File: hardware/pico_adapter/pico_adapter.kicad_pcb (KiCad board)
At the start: 2 copper layers, 13 x 1.4 mm, 43 parts, among them J1 L77HDE15SD1CH4F, J2 AudioJack2_Ground, J3 5V in, Q1 Q_NMOS_DGS, Q2 Q_NMOS_DGS

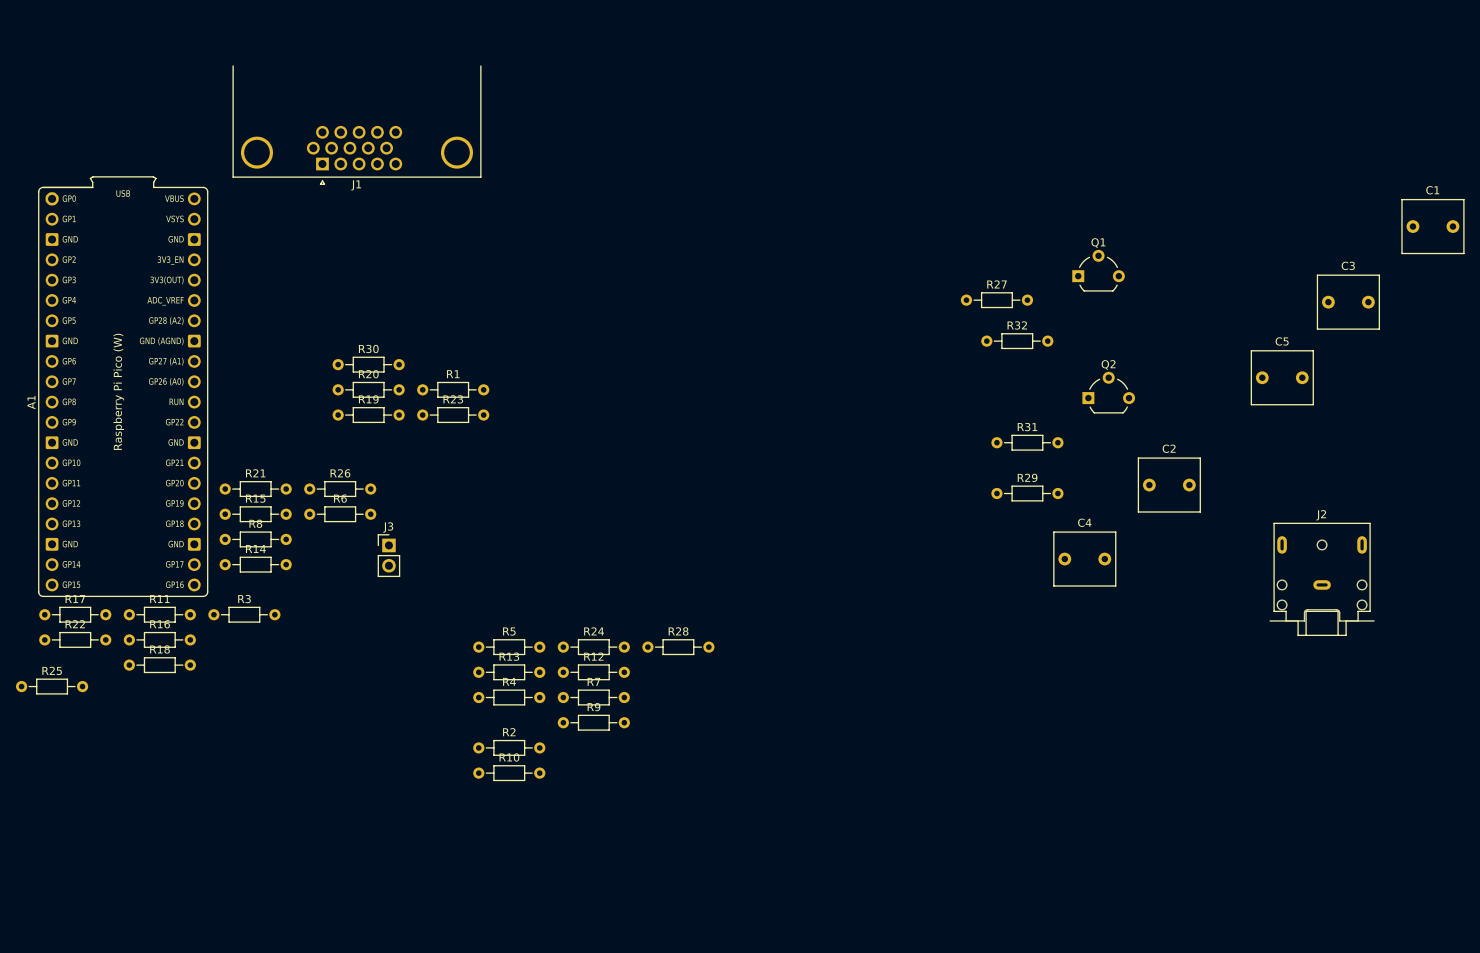
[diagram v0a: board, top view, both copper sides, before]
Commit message: fixed PWR_FLAG in schematic, problem: layout GND area does not fill
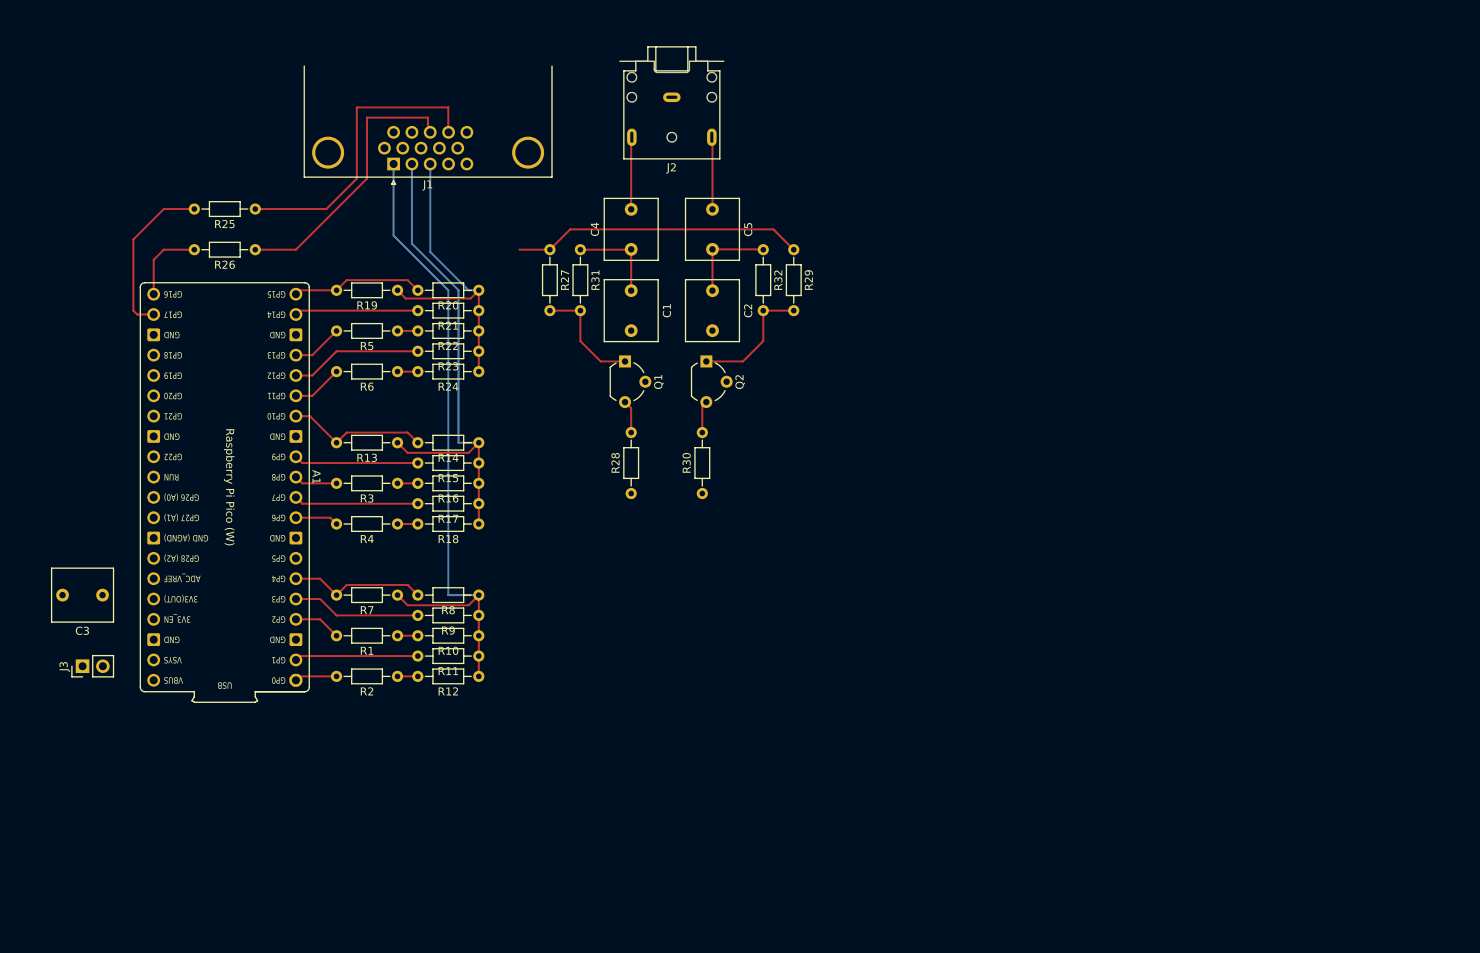
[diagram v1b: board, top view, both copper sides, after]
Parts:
- A1: value RaspberryPi-Pico_Socket -> RaspberryPi-Pico-Socket
- moved C3 157.5 mm to (39.3, 92.7), turned to 180 degrees
- moved J2 101.6 mm to (110.5, 30.5), turned to 180 degrees
- moved C1 98.0 mm to (105.4, 54.6), turned to -90 degrees
- moved C5 71.9 mm to (115.6, 44.5), turned to -90 degrees
- moved A1 67.5 mm to (63.5, 103.4), turned to 180 degrees
- moved C4 66.6 mm to (105.4, 49.5), turned to 90 degrees
- moved R22 66.6 mm to (86.4, 59.7), turned to 180 degrees
- moved R25 66.5 mm to (58.4, 44.5), turned to 180 degrees
- moved C2 59.8 mm to (115.6, 54.6), turned to -90 degrees
- moved Q1 57.6 mm to (104.6, 63.5), turned to -90 degrees
- moved R31 57.4 mm to (99.1, 49.5), turned to -90 degrees
- moved R17 56.0 mm to (86.4, 81.3), turned to 180 degrees
- moved R27 52.5 mm to (95.2, 49.5), turned to -90 degrees
- moved R30 48.3 mm to (114.3, 80.0), turned to 90 degrees
- moved Q2 48.0 mm to (114.8, 63.5), turned to -90 degrees
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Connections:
- A1 pad 39: unconnected-(A1-Pad39) -> +5V
- A1 pad 40: +5V -> unconnected-(A1-Pad40)
- R13 pad 2: /GPIO4 -> /GPIO10
- R14 pad 2: /GPIO4 -> /GPIO10
- R15 pad 2: /GPIO3 -> /GPIO9
- R17 pad 2: /GPIO1 -> /GPIO7
- R19 pad 2: /GPIO4 -> /GPIO15
- R20 pad 2: /GPIO4 -> /GPIO15
- R21 pad 2: /GPIO3 -> /GPIO14
- R23 pad 2: /GPIO1 -> /GPIO12
- R3 pad 2: /GPIO2 -> /GPIO8
- R4 pad 2: /GPIO0 -> /GPIO6
- R5 pad 2: /GPIO2 -> /GPIO13
- R6 pad 2: /GPIO0 -> /GPIO11
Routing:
- net /VGA_R: track 0.00 -> 81.9 mm
- net /VGA_G: track 0.00 -> 61.2 mm
- net /VGA_B: track 0.00 -> 40.2 mm
- net /VSYNC: track 0.00 -> 37.1 mm
- net +3V3: track 0.00 -> 36.4 mm
- net /HSYNC: track 0.00 -> 34.2 mm
- net Net-(A1-Pad22): track 0.00 -> 20.8 mm
- net /GPIO10: track 0.00 -> 17.7 mm
- net /GPIO4: track 0.00 -> 17.1 mm
- net /GPIO12: track 0.00 -> 16.5 mm
- net /GPIO15: track 0.00 -> 16.5 mm
- net /GPIO3: track 0.00 -> 16.1 mm
- net Net-(Q2-Pad1): track 0.00 -> 15.8 mm
- net /GPIO9: track 0.00 -> 15.6 mm
- net /GPIO7: track 0.00 -> 15.6 mm
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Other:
- outline, holes or cut-outs redrawn

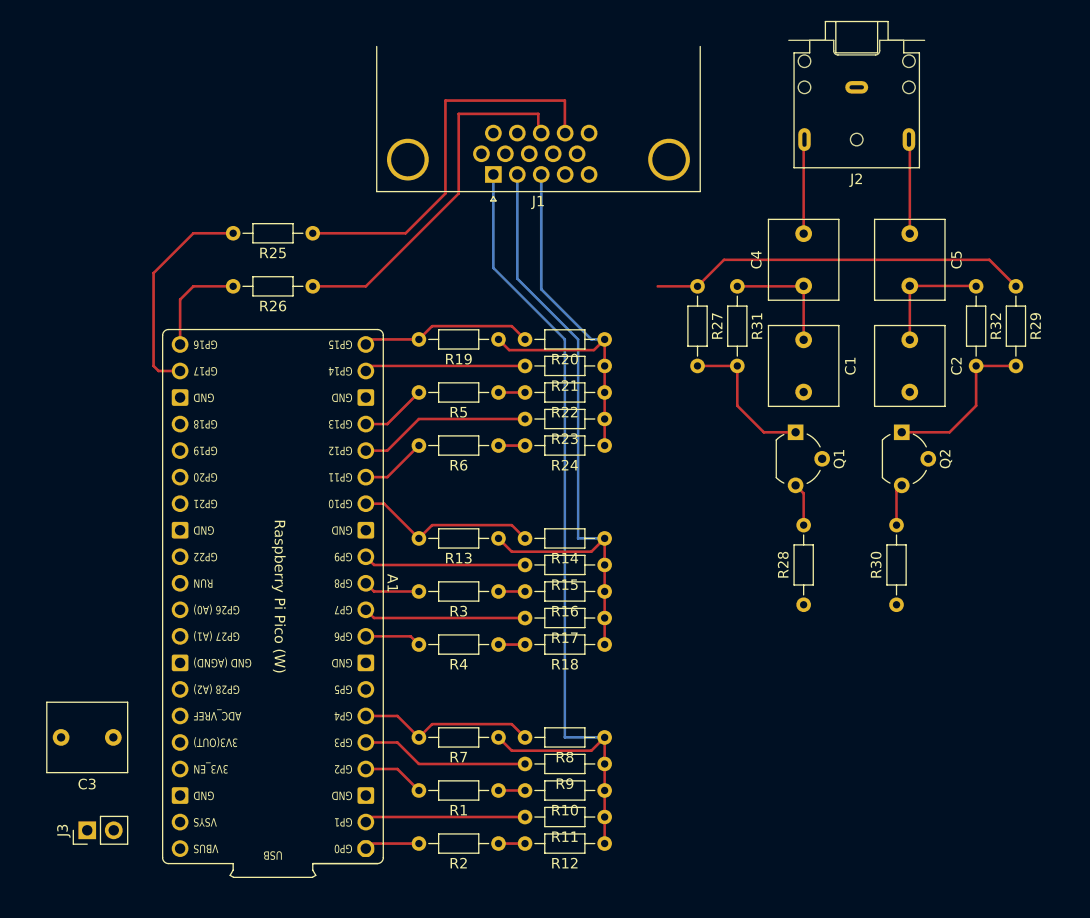
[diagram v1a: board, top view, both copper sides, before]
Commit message: GND area does fill now, still DRC errors
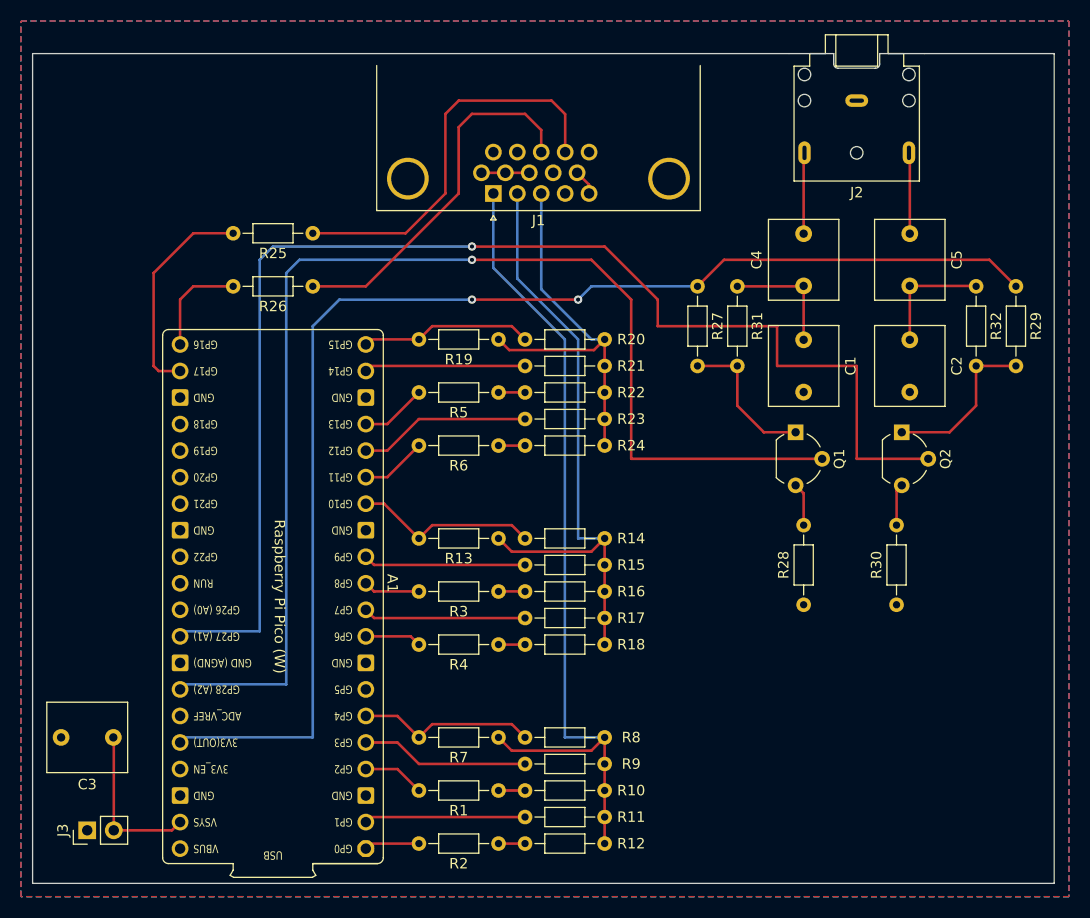
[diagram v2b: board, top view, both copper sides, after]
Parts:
- J2: value AudioJack2_Ground -> AudioJack3
- moved J1 1.82 mm to (75.7, 40.6)
- moved J2 1.27 mm to (110.5, 31.8)
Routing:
- net /PWM_R: track 0.00 -> 125.3 mm, vias 0 -> 1
- net /PWM_L: track 0.00 -> 118.7 mm, vias 0 -> 1
- net +3V3: track 36.4 -> 123.5 mm, vias 0 -> 2
- net +5V: track 0.00 -> 15.6 mm
- net GND: track 0.00 -> 7.03 mm
- net /VGA_R: track 81.9 -> 80.1 mm
- net /VGA_G: track 61.2 -> 59.3 mm
- net /VGA_B: track 40.2 -> 38.4 mm
- net Net-(C5-Pad1): track 9.04 -> 7.77 mm
- net Net-(C4-Pad2): track 9.04 -> 7.77 mm
- net /HSYNC: track 34.2 -> 35.2 mm
- net /VSYNC: track 37.1 -> 38.1 mm
- added copper zone on B.Cu, net GND
- added copper zone on F.Cu, net GND
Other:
- board size 13 x 1.4 mm -> 97.8 x 79.4 mm

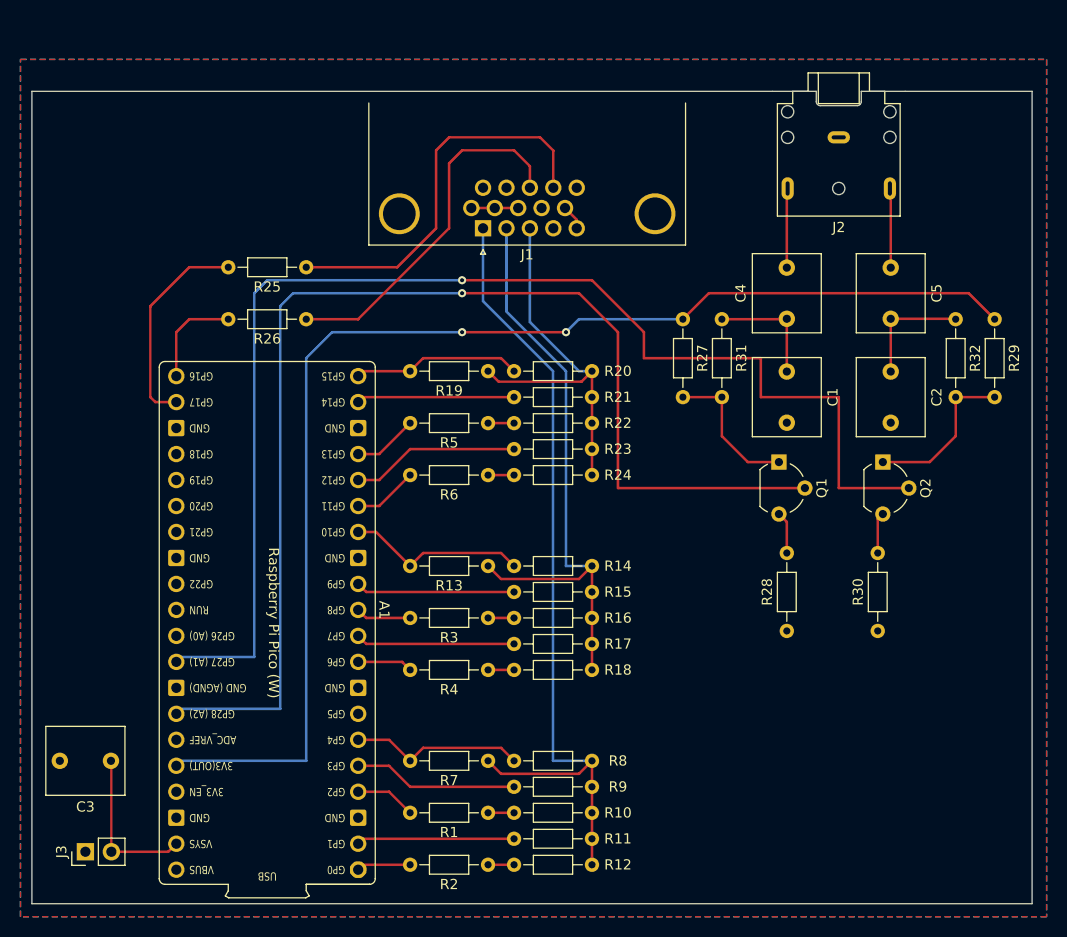
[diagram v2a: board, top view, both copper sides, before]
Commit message: changed 3.5mm socket
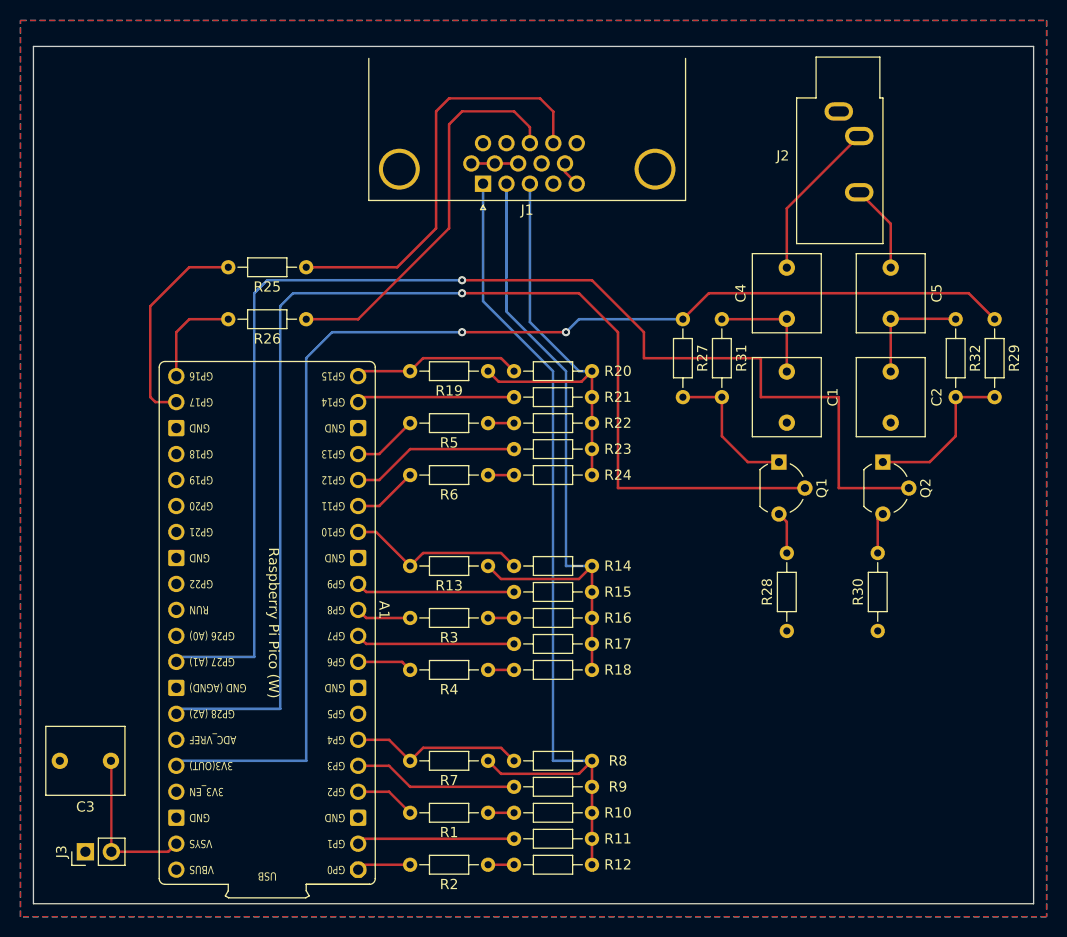
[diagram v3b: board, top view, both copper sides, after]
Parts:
- J2: footprint Connector_Audio:Jack_3.5mm_CUI_SJ1-3523N_Horizontal -> Connector_Audio:Jack_3.5mm_CUI_SJ1-3533NG_Horizontal
- moved J1 4.36 mm to (75.7, 36.3)
- moved J2 2.53 mm to (110.5, 29.2), turned to 0 degrees
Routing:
- net Net-(C4-Pad2): track 7.77 -> 15.8 mm
- net /VGA_R: track 80.1 -> 84.4 mm
- net /VGA_G: track 59.3 -> 63.7 mm
- net /VGA_B: track 38.4 -> 42.8 mm
- net /VSYNC: track 38.1 -> 41.3 mm
- net /HSYNC: track 35.2 -> 38.4 mm
- net Net-(C5-Pad1): track 7.77 -> 8.65 mm
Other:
- board size 97.8 x 79.4 mm -> 97.8 x 83.8 mm
